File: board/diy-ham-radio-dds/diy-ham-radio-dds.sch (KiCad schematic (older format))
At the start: 63 parts, among them J1 ICSP, J2 I2C, J3 VCC, J4 NPN OUT, J5 , J6 UART_PROG, Q1 S0805, Q2 S0805, Q3 S0805, Q4 S0805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

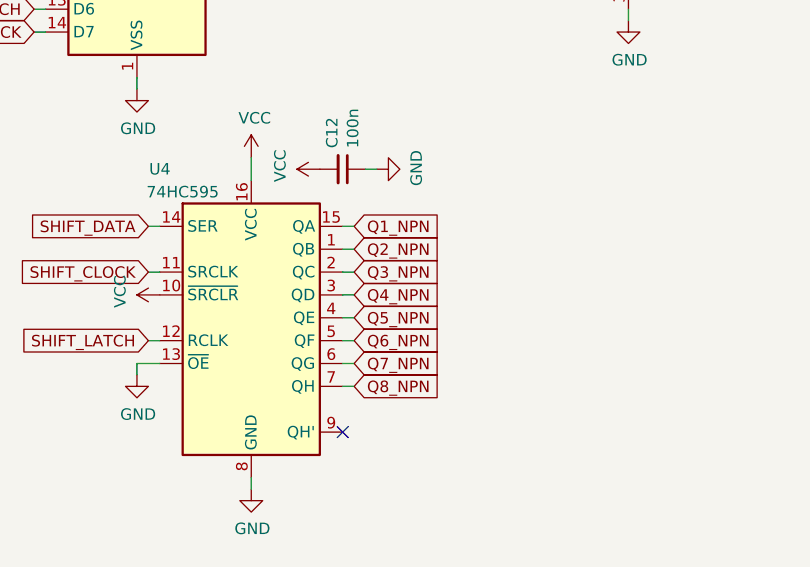
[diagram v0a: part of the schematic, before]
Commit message: Changed NPN out channels in schematics
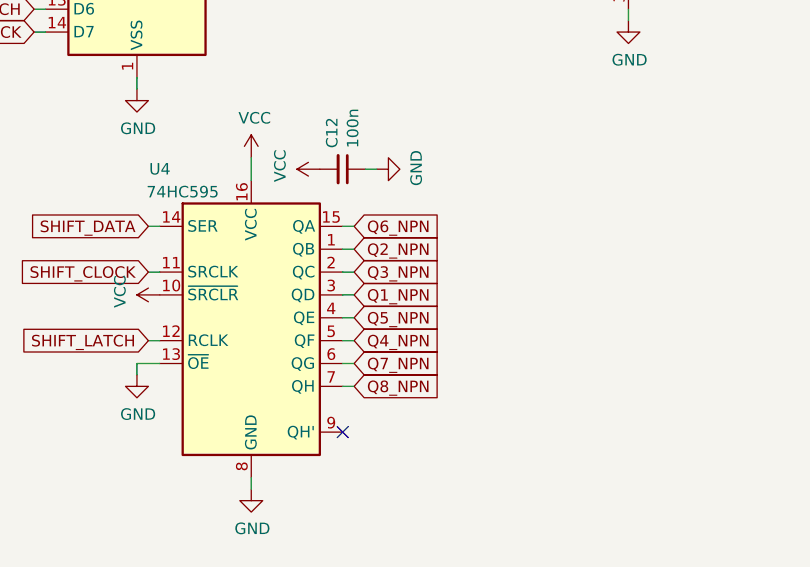
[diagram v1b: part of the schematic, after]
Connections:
- net Q1_NPN: now also U4.3 (QD); no longer U4.15 (QA)
- net Q4_NPN: now also U4.5 (QF); no longer U4.3 (QD)
- net Q6_NPN: now also U4.15 (QA); no longer U4.5 (QF)
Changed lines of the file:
@@
 Text GLabel 9950 4650 0    50   Input ~ 0
 ALARM
-Text GLabel 5800 6350 2    50   Input ~ 0
+Text GLabel 5800 6650 2    50   Input ~ 0
 Q1_NPN
 Text GLabel 5800 6450 2    50   Input ~ 0
@@
 Text GLabel 5800 6550 2    50   Input ~ 0
 Q3_NPN
-Text GLabel 5800 6650 2    50   Input ~ 0
+Text GLabel 5800 6850 2    50   Input ~ 0
 Q4_NPN
 Text GLabel 5800 6750 2    50   Input ~ 0
 Q5_NPN
-Text GLabel 5800 6850 2    50   Input ~ 0
+Text GLabel 5800 6350 2    50   Input ~ 0
 Q6_NPN
 Text GLabel 5800 6950 2    50   Input ~ 0

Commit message: Finalised board drawing
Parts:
- J1: footprint Connector_PinHeader_1.00mm:PinHeader_2x03_P1.00mm_Vertical -> Connector_PinHeader_2.54mm:PinHeader_2x03_P2.54mm_Vertical
- J2, J3: footprint Connector_PinHeader_1.00mm:PinHeader_2x04_P1.00mm_Vertical -> Connector_PinHeader_2.54mm:PinHeader_2x04_P2.54mm_Vertical
- J6: footprint Connector_PinHeader_1.27mm:PinHeader_1x06_P1.27mm_Vertical -> Connector_PinHeader_2.54mm:PinHeader_1x06_P2.54mm_Vertical
- RV1: footprint Potentiometer_THT:Potentiometer_Alpha_RD901F-40-00D_Single_Vertical -> Potentiometer_THT:Potentiometer_Bourns_3296W_Vertical
- U3: footprint Package_TO_SOT_THT:TO-220-3_Vertical -> Package_TO_SOT_THT:TO-220-3_Horizontal_TabDown
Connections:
- net GND: now also J5.10 (Pin_10)
- net POT1_A: now also J5.6 (Pin_6); no longer J5.4 (Pin_4)
- net POT1_C: now also J5.4 (Pin_4); no longer J5.6 (Pin_6)
- net POT2_A: now also J5.3 (Pin_3); no longer J5.1 (Pin_1)
- net POT2_C: now also J5.1 (Pin_1); no longer J5.3 (Pin_3)
- net POT_1: now also U1.22 (ADC7); no longer U1.19 (ADC6)
- net POT_2: now also U1.19 (ADC6); no longer U1.22 (ADC7)
- net Q1_NPN: now also U4.2 (QC); no longer U4.3 (QD)
- net Q3_NPN: now also U4.3 (QD); no longer U4.2 (QC)
- net VIN: now also J5.9 (Pin_9)
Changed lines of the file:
@@
 F 0 "U3" H 1700 1392 50  0000 C CNN
 F 1 "L7805" H 1700 1301 50  0000 C CNN
-F 2 "Package_TO_SOT_THT:TO-220-3_Vertical" H 1725 1000 50  0001 L CIN
+F 2 "Package_TO_SOT_THT:TO-220-3_Horizontal_TabDown" H 1725 1000 50  0001 L CIN
 F 3 "http://www.st.com/content/ccc/resource/technical/document/datasheet/41/4f/b3/b0/12/d4/47/88/CD00000444.pdf/files/CD00000444.pdf/jcr:content/translations/en.CD00000444.pdf" H 1700 1100 50  0001 C CNN
 	1    1700 1150
@@
 F 0 "RV1" H 5030 3546 50  0000 R CNN
 F 1 "10k" H 5030 3455 50  0000 R CNN
-F 2 "Potentiometer_THT:Potentiometer_Alpha_RD901F-40-00D_Single_Vertical" H 5100 3500 50  0001 C CNN
+F 2 "Potentiometer_THT:Potentiometer_Bourns_3296W_Vertical" H 5100 3500 50  0001 C CNN
 F 3 "~" H 5100 3500 50  0001 C CNN
 	1    5100 3500
@@
 Text GLabel 2200 3500 2    50   Input ~ 0
 SW4
+Text GLabel 900  3400 0    50   Input ~ 0
+POT_1
 Text GLabel 900  3300 0    50   Input ~ 0
-POT_1
-Text GLabel 900  3400 0    50   Input ~ 0
 POT_2
 Text GLabel 2200 3100 2    50   Input ~ 0
@@
 F 0 "J1" H 10100 1417 50  0000 C CNN
 F 1 "ICSP" H 10100 1326 50  0000 C CNN
-F 2 "Connector_PinHeader_1.00mm:PinHeader_2x03_P1.00mm_Vertical" H 10050 1100 50  0001 C CNN
+F 2 "Connector_PinHeader_2.54mm:PinHeader_2x03_P2.54mm_Vertical" H 10050 1100 50  0001 C CNN
 F 3 "~" H 10050 1100 50  0001 C CNN
 	1    10050 1100
@@
 F 0 "J2" H 10100 2167 50  0000 C CNN
 F 1 "I2C" H 10100 2076 50  0000 C CNN
-F 2 "Connector_PinHeader_1.00mm:PinHeader_2x04_P1.00mm_Vertical" H 10050 1850 50  0001 C CNN
+F 2 "Connector_PinHeader_2.54mm:PinHeader_2x04_P2.54mm_Vertical" H 10050 1850 50  0001 C CNN
 F 3 "~" H 10050 1850 50  0001 C CNN
 	1    10050 1850
@@
 F 0 "J3" H 10100 2817 50  0000 C CNN
 F 1 "VCC" H 10100 2726 50  0000 C CNN
-F 2 "Connector_PinHeader_1.00mm:PinHeader_2x04_P1.00mm_Vertical" H 10050 2500 50  0001 C CNN
+F 2 "Connector_PinHeader_2.54mm:PinHeader_2x04_P2.54mm_Vertical" H 10050 2500 50  0001 C CNN
 F 3 "~" H 10050 2500 50  0001 C CNN
 	1    10050 2500
@@
 Text GLabel 9500 4000 0    50   Input ~ 0
 GND
-Text GLabel 9950 4250 0    50   Input ~ 0
-POT1_A
 Text GLabel 9950 4350 0    50   Input ~ 0
 POT1_B
-Text GLabel 9950 4450 0    50   Input ~ 0
-POT1_C
-Text GLabel 9950 3950 0    50   Input ~ 0
+Text GLabel 9950 4150 0    50   Input ~ 0
 POT2_A
 Text GLabel 9950 4050 0    50   Input ~ 0
 POT2_B
-Text GLabel 9950 4150 0    50   Input ~ 0
+Text GLabel 9950 3950 0    50   Input ~ 0
 POT2_C
 $Comp
@@
 Text GLabel 9950 4650 0    50   Input ~ 0
 ALARM
-Text GLabel 5800 6650 2    50   Input ~ 0
+Text GLabel 5800 6550 2    50   Input ~ 0
 Q1_NPN
 Text GLabel 5800 6450 2    50   Input ~ 0
 Q2_NPN
-Text GLabel 5800 6550 2    50   Input ~ 0
+Text GLabel 5800 6650 2    50   Input ~ 0
 Q3_NPN
 Text GLabel 5800 6850 2    50   Input ~ 0
@@
 	9950 4650 10000 4650
 Wire Wire Line
-	9950 4750 10000 4750
-Wire Wire Line
-	9950 4850 10000 4850
-Wire Wire Line
 	10350 1100 10400 1100
 Text GLabel 10400 1100 2    50   Input ~ 0
@@
 F 0 "J6" H 10280 5392 50  0000 L CNN
 F 1 "UART_PROG" H 10280 5301 50  0000 L CNN
-F 2 "Connector_PinHeader_1.27mm:PinHeader_1x06_P1.27mm_Vertical" H 10200 5400 50  0001 C CNN
+F 2 "Connector_PinHeader_2.54mm:PinHeader_1x06_P2.54mm_Vertical" H 10200 5400 50  0001 C CNN
 F 3 "~" H 10200 5400 50  0001 C CNN
 	1    10200 5400
@@
 NoConn ~ 4200 2050
 NoConn ~ 4350 1450
+$Comp
+L power:GND #PWR0101
+U 1 1 601EB40E
+P 9350 4900
+F 0 "#PWR0101" H 9350 4650 50  0001 C CNN
+F 1 "GND" H 9355 4727 50  0000 C CNN
+F 2 "" H 9350 4900 50  0001 C CNN
+F 3 "" H 9350 4900 50  0001 C CNN
+	1    9350 4900
+	1    0    0    -1
+$EndComp
+Text GLabel 9350 4750 0    50   Input ~ 0
+VIN
+Wire Wire Line
+	9350 4750 10000 4750
+Wire Wire Line
+	9350 4900 9350 4850
+Wire Wire Line
+	9350 4850 10000 4850
+Text GLabel 9950 4250 0    50   Input ~ 0
+POT1_C
+Text GLabel 9950 4450 0    50   Input ~ 0
+POT1_A
 $EndSCHEMATC
